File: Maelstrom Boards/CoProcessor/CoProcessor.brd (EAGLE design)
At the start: 101.6 x 101.6 mm, 2 parts, among them U1 STM32F439ZIT6

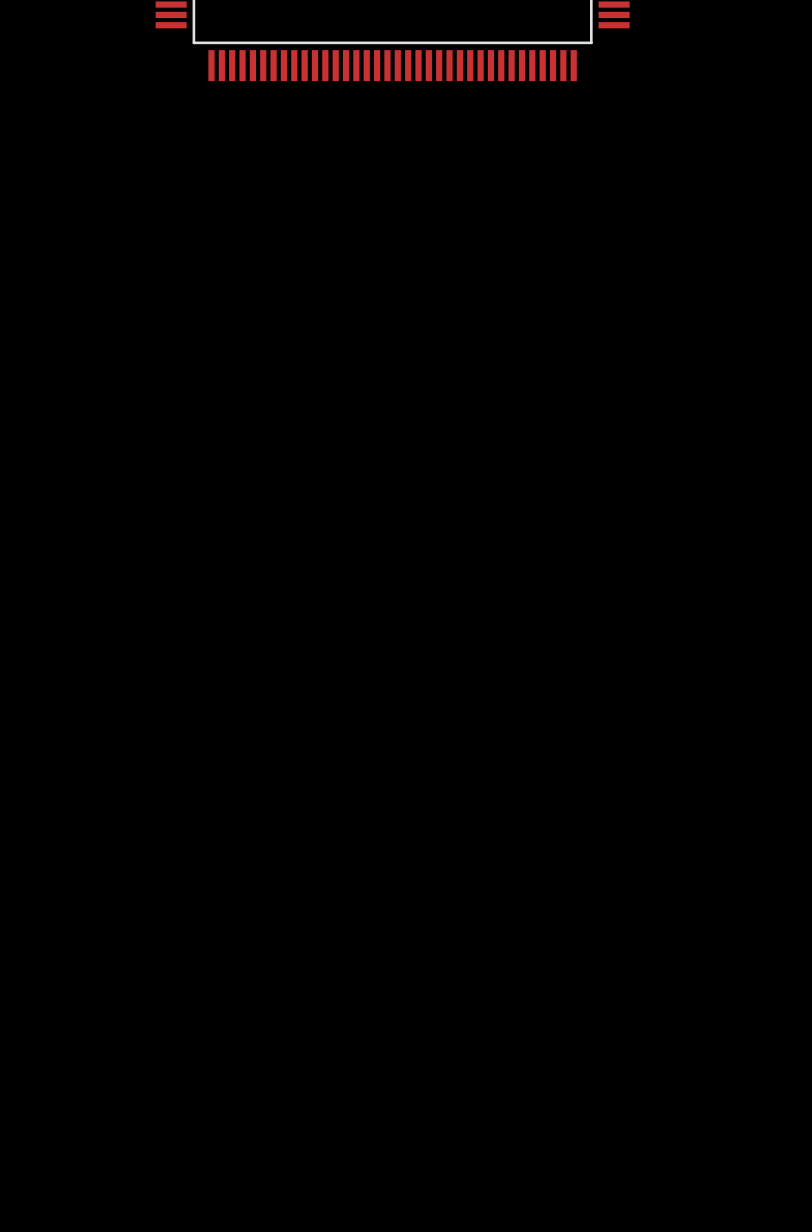
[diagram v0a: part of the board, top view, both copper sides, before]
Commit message: add base copro requirements
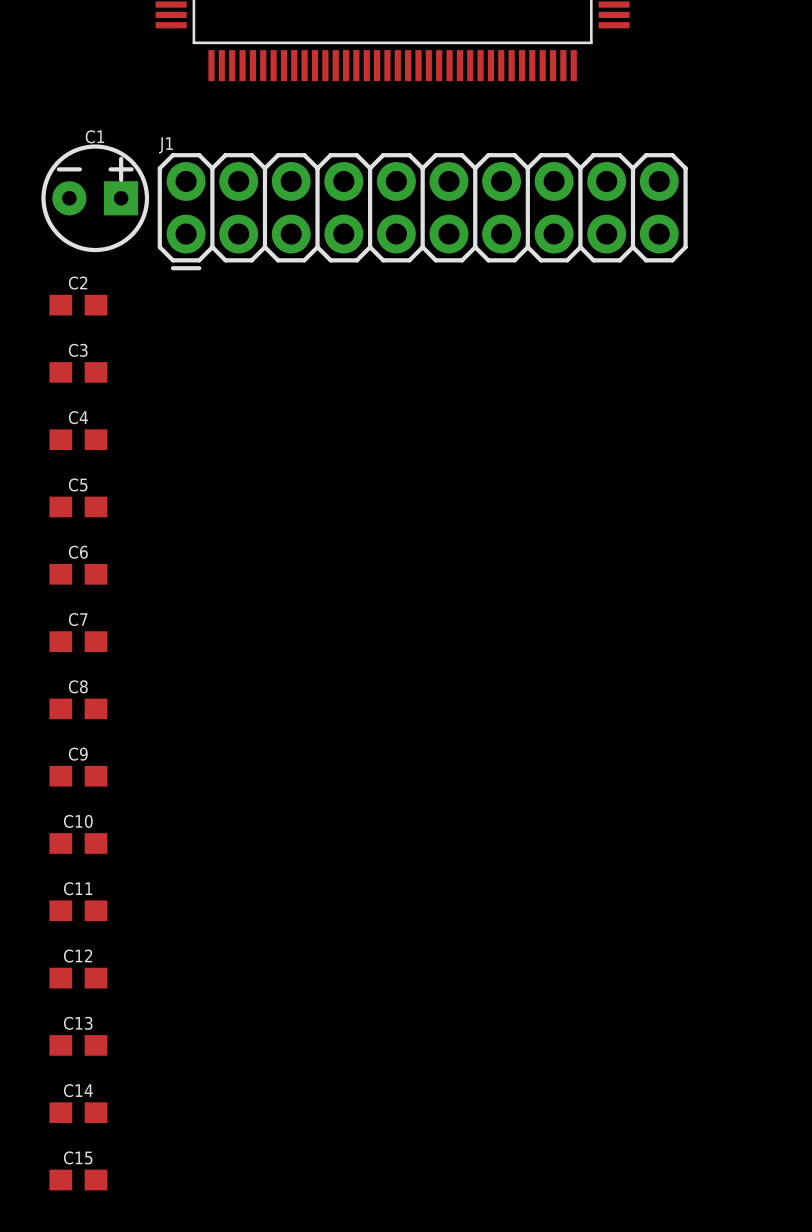
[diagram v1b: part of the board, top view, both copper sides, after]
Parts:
- added C1: 10uF, SparkFun-Capacitors:CPOL-RADIAL-2.5MM-5MM-KIT
- added C10, C11, C12, C13, C2, C3, C4, C5, C6, C7, C8, C9: 0.1uF, SparkFun-Capacitors:0603
- added C14, C15: 2.2uF, SparkFun-Capacitors:0603
- added J1: (no value), SparkFun-Connectors:2X10
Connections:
- removed net VCAP_1: U1.71
- removed net VCAP_2: U1.106
- removed net VDD: U1.108, U1.121, U1.131, U1.144, U1.17, U1.30, U1.39, U1.52, U1.62, U1.72, U1.84, U1.95
- removed net VSS: U1.107, U1.120, U1.130, U1.16, U1.38, U1.51, U1.61, U1.83, U1.94
- new net 3V3PWR: C1.1, C10.1, C11.1, C12.1, C13.1, C2.1, C3.1, C4.1, C5.1, C6.1, C7.1, C8.1, C9.1, J1.1, J1.2, U$1.4, U$1.5, U$1.51, U$1.52, U$1.53, U$1.6, U1.108, U1.121, U1.131, U1.144, U1.17, U1.30, U1.39, U1.52, U1.62, U1.72, U1.84, U1.95
- new net 5VPWR: U$1.1, U$1.2, U$1.3, U$1.54, U$1.55, U$1.56
- new net GND: C1.2, C10.2, C11.2, C12.2, C13.2, C14.2, C15.2, C2.2, C3.2, C4.2, C5.2, C6.2, C7.2, C8.2, C9.2, J1.10, J1.12, J1.14, J1.16, J1.18, J1.20, J1.4, J1.6, J1.8, U$1.48, U$1.49, U$1.50, U$1.7, U$1.8, U$1.9, U1.107, U1.120, U1.130, U1.16, U1.38, U1.51, U1.61, U1.83, U1.94
- new net JTCK: J1.9, U1.109
- new net JTDI: J1.5, U1.110
- new net JTDO: J1.13, U1.133
- new net JTMS: J1.7, U1.105
- new net JTRST: J1.3, U1.134
- new net N$1: C14.1, U1.106
- new net N$2: C15.1, U1.71
- new net NRST: J1.15, U1.25

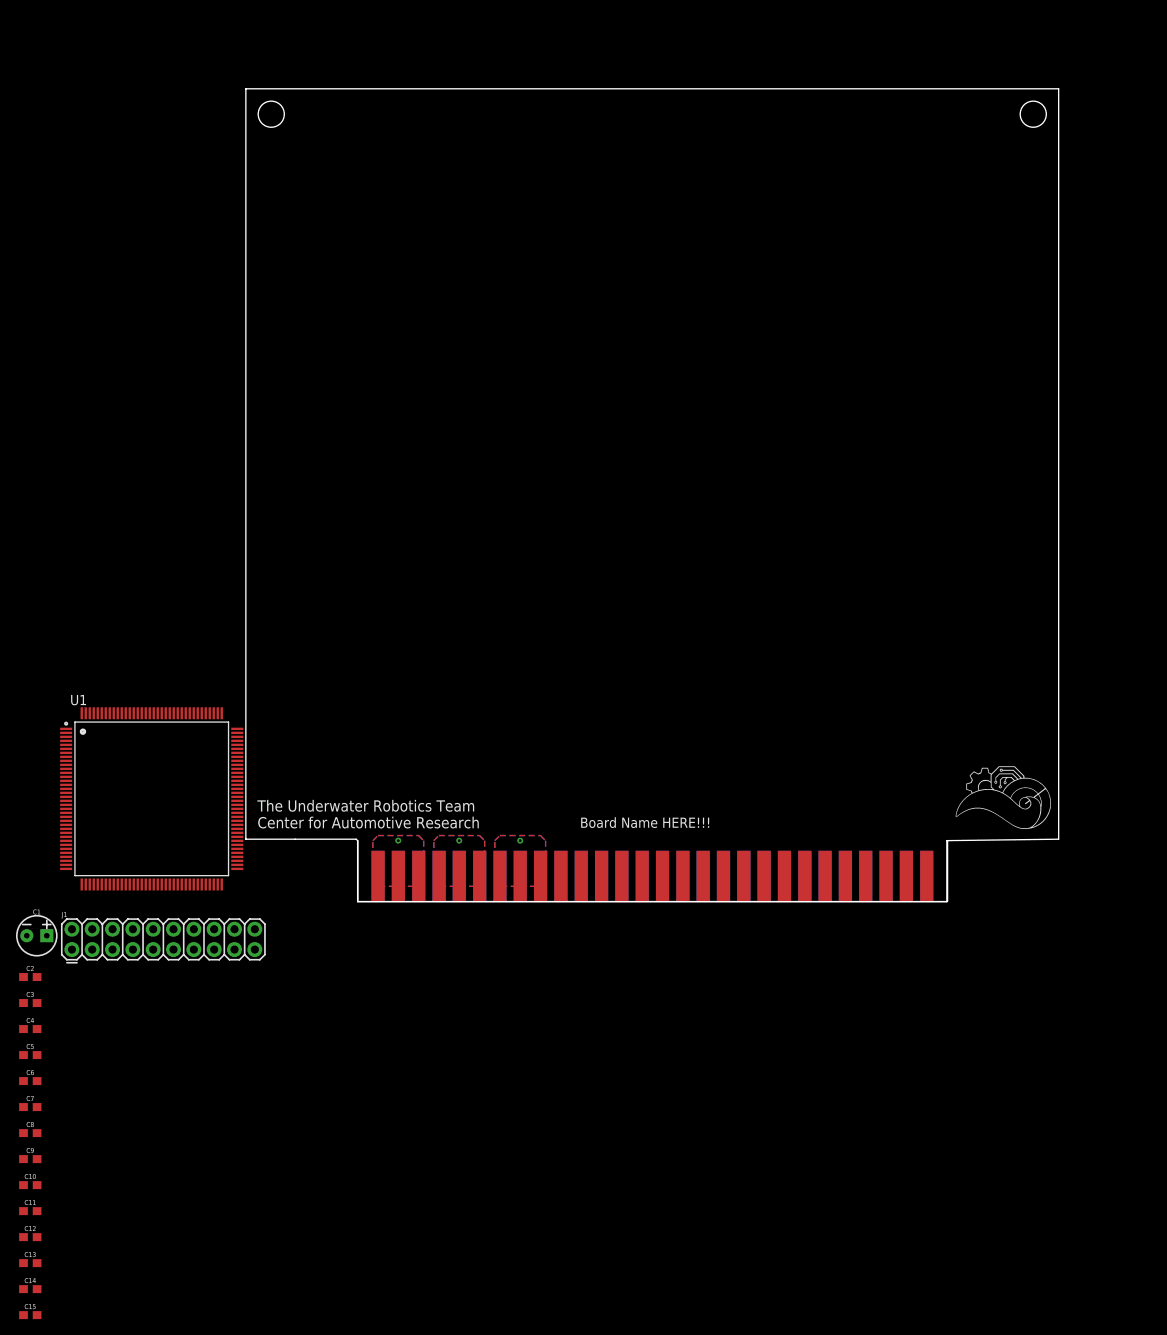
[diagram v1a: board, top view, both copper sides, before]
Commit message: Almost done with schematic, working on board
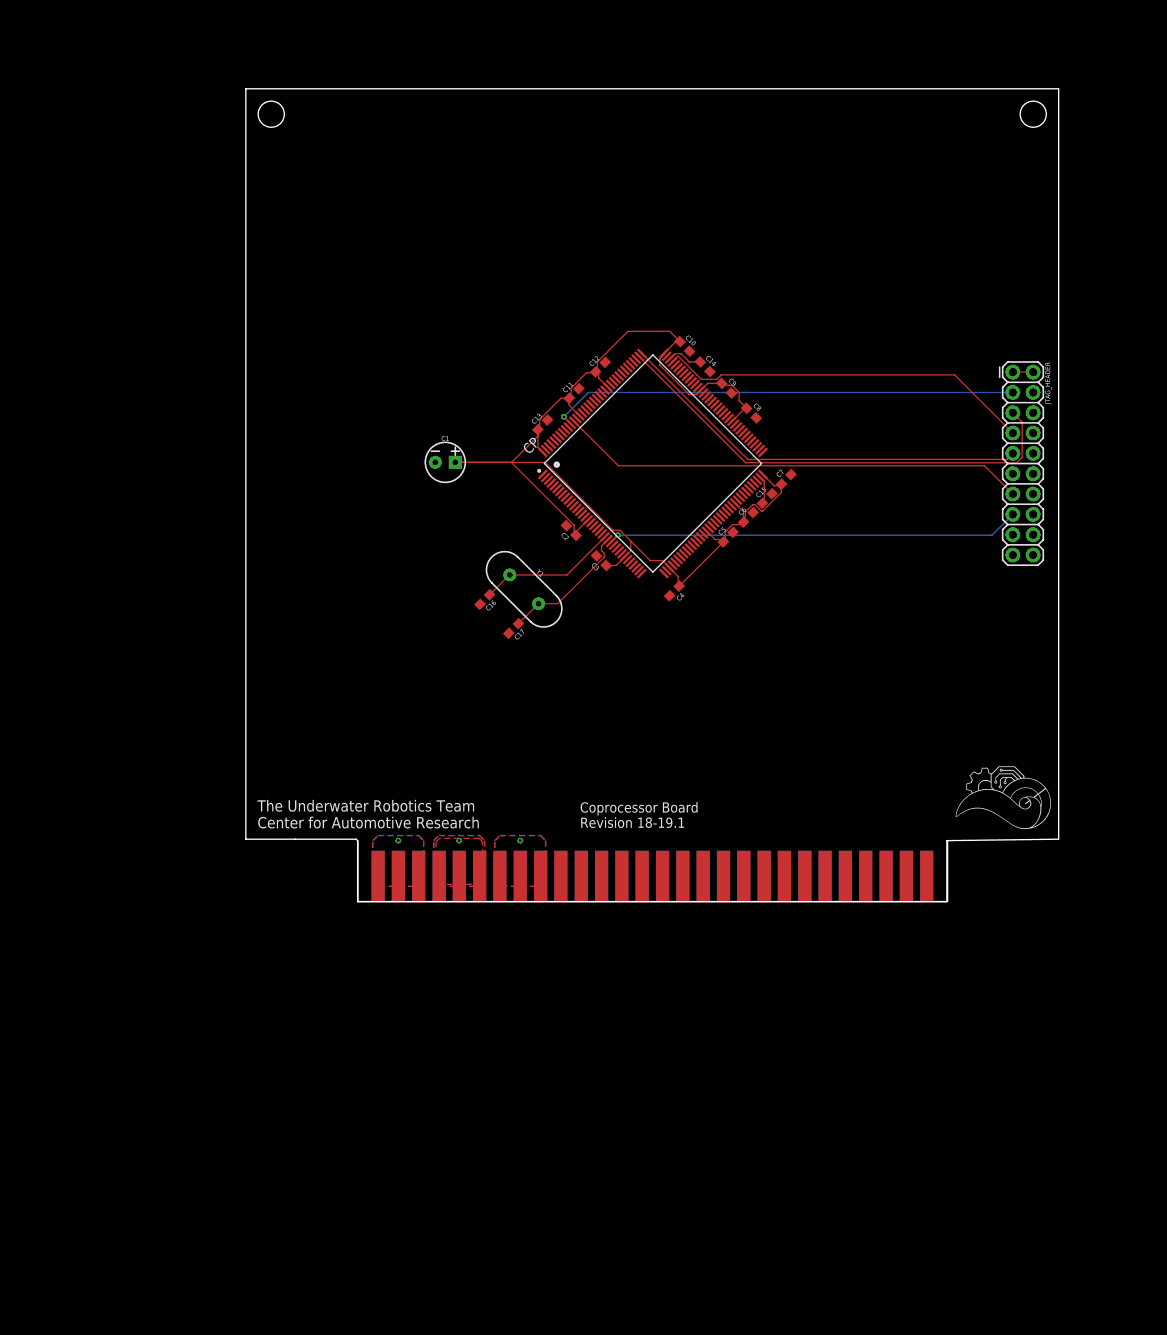
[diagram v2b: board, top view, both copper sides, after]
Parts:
- removed J1: (no value), SparkFun-Connectors:2X10
- removed U1: STM32F439ZIT6, STM32F439ZIT6:QFP50P2200X2200X160-144N
- added C16, C17: 18pF, SparkFun-Capacitors:0603
- added CP: STM32F439ZIT6, STM32F439ZIT6:QFP50P2200X2200X160-144N
- added JTAG_HEADER: (no value), SparkFun-Connectors:2X10
- added Y1: (no value), SparkFun-Clocks:HC49US
- moved C14 142.9 mm to (57.4, 66.9), turned to 315 degrees
- moved C15 137.5 mm to (65.2, 50.4), turned to 45 degrees
- moved C10 133.0 mm to (54.9, 69.4), turned to 315 degrees
- moved C12 130.0 mm to (44.3, 66.8), turned to 45 degrees
- moved C9 129.8 mm to (60.1, 64.2), turned to 315 degrees
- moved C8 127.4 mm to (63.2, 61.1), turned to 315 degrees
- moved C7 122.8 mm to (67.5, 52.8), turned to 45 degrees
- moved C13 122.8 mm to (37.1, 59.6), turned to 45 degrees
- moved C11 122.7 mm to (41.0, 63.5), turned to 45 degrees
- moved C6 114.1 mm to (62.8, 48.0), turned to 45 degrees
- moved C5 108.6 mm to (60.3, 45.6), turned to 45 degrees
- moved C4 97.4 mm to (53.6, 38.8), turned to 225 degrees
- moved C3 90.3 mm to (44.4, 42.6), turned to 135 degrees
- moved C2 87.7 mm to (40.7, 46.4), turned to 135 degrees
- moved C1 78.2 mm to (24.9, 54.9)
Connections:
- new net OSC1: C17.1, CP.24, Y1.2
- new net OSC2: C16.1, CP.23, Y1.1
- net 3V3PWR: now also CP.108, CP.121, CP.131, CP.144, CP.17, CP.30, CP.39, CP.52, CP.62, CP.72, CP.84, CP.95, JTAG_HEADER.1, JTAG_HEADER.2; no longer J1.1, J1.2, U1.108, U1.121, U1.131, U1.144, U1.17, U1.30, U1.39, U1.52, U1.62, U1.72, U1.84, U1.95
- net GND: now also C16.2, C17.2, CP.107, CP.120, CP.130, CP.16, CP.38, CP.51, CP.61, CP.83, CP.94, JTAG_HEADER.10, JTAG_HEADER.12, JTAG_HEADER.14, JTAG_HEADER.16, JTAG_HEADER.18, JTAG_HEADER.20, JTAG_HEADER.4, JTAG_HEADER.6, JTAG_HEADER.8; no longer J1.10, J1.12, J1.14, J1.16, J1.18, J1.20, J1.4, J1.6, J1.8, U1.107, U1.120, U1.130, U1.16, U1.38, U1.51, U1.61, U1.83, U1.94
- net JTCK: now also CP.109, JTAG_HEADER.9; no longer J1.9, U1.109
- net JTDI: now also CP.110, JTAG_HEADER.5; no longer J1.5, U1.110
- net JTDO: now also CP.133, JTAG_HEADER.13; no longer J1.13, U1.133
- net JTMS: now also CP.105, JTAG_HEADER.7; no longer J1.7, U1.105
- net JTRST: now also CP.134, JTAG_HEADER.3; no longer J1.3, U1.134
- net N$1: now also CP.106; no longer U1.106
- net N$2: now also CP.71; no longer U1.71
- net NRST: now also CP.25, JTAG_HEADER.15; no longer J1.15, U1.25
- net PDR_ON: now also CP.143; no longer U1.143
- net VBAT: now also CP.6; no longer U1.6
- net VDDA: now also CP.33; no longer U1.33
- net VREF+: now also CP.32; no longer U1.32
- net VSSA: now also CP.31; no longer U1.31
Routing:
- net 3V3PWR: track 0.00 -> 157.8 mm
- net JTDI: track 0.00 -> 59.7 mm
- net JTRST: track 0.00 -> 58.7 mm, vias 0 -> 1
- net JTDO: track 0.00 -> 58.6 mm
- net JTCK: track 0.00 -> 52.2 mm
- net NRST: track 0.00 -> 51.7 mm, vias 0 -> 1
- net JTMS: track 0.00 -> 47.3 mm
- net OSC2: track 0.00 -> 17.4 mm
- net OSC1: track 0.00 -> 17.0 mm
- net N$1: track 0.00 -> 4.54 mm
- net N$2: track 0.00 -> 3.54 mm
- added copper zone on layer 1, net 3V3PWR
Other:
- board text added: "Coprocessor Board Revision 18-19.1"
- board text removed: "Board Name HERE!!!"

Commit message: Update copro for f405
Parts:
- removed C1: 10uF, SparkFun-Capacitors:CPOL-RADIAL-2.5MM-5MM-KIT
- removed C10, C11, C12, C13, C2, C3, C4, C5, C6, C7, C8, C9: 0.1uF, SparkFun-Capacitors:0603
- removed C14, C15: 2.2uF, SparkFun-Capacitors:0603
- removed C16, C17: 18pF, SparkFun-Capacitors:0603
- removed CP: STM32F439ZIT6, STM32F439ZIT6:QFP50P2200X2200X160-144N
- removed JTAG_HEADER: (no value), SparkFun-Connectors:2X10
- removed Y1: (no value), SparkFun-Clocks:HC49US
- added U1: STM32F405RGT6, STM32F405RGT6:QFP50P1200X1200X160-64N
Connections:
- net 5VPWR renamed +3V3
- removed net 3V3PWR: C1.1, C10.1, C11.1, C12.1, C13.1, C2.1, C3.1, C4.1, C5.1, C6.1, C7.1, C8.1, C9.1, CP.108, CP.121, CP.131, CP.144, CP.17, CP.30, CP.39, CP.52, CP.62, CP.72, CP.84, CP.95, JTAG_HEADER.1, JTAG_HEADER.2, U$1.4, U$1.5, U$1.51, U$1.52, U$1.53, U$1.6
- removed net JTCK: CP.109, JTAG_HEADER.9
- removed net JTDI: CP.110, JTAG_HEADER.5
- removed net JTDO: CP.133, JTAG_HEADER.13
- removed net JTMS: CP.105, JTAG_HEADER.7
- removed net JTRST: CP.134, JTAG_HEADER.3
- removed net N$1: C14.1, CP.106
- removed net N$2: C15.1, CP.71
- removed net NRST: CP.25, JTAG_HEADER.15
- removed net OSC1: C17.1, CP.24, Y1.2
- removed net OSC2: C16.1, CP.23, Y1.1
- removed net PDR_ON: CP.143
- removed net VREF+: CP.32
- new net +5V: U$1.11, U$1.12, U$1.13, U$1.44, U$1.45, U$1.46
- new net 12V_CNTRL: U$1.16
- new net 3V3_CNTRL: U$1.14
- new net 5V_CNTRL: U$1.15
- new net ACOUS_CNTRL: U$1.17
- new net BOARD_SCL: U$1.31
- new net BOARD_SDA: U$1.32
- new net JETS_CNTRL: U$1.18
- new net MOBO_CNTRL: U$1.19
- new net PWM_CH1: U$1.20
- new net PWM_CH2: U$1.21
- new net PWM_CH3: U$1.22
- new net PWM_CH4: U$1.23
- new net PWM_CH5: U$1.24
- new net PWM_CH6: U$1.25
- new net PWM_CH7: U$1.26
- new net PWM_CH8: U$1.27
- new net SENSOR_SCL: U$1.29
- new net SENSOR_SDA: U$1.30
- new net SW_1: U$1.38
- new net SW_2: U$1.39
- new net SW_3: U$1.40
- new net SW_4: U$1.41
- new net SW_5: U$1.42
- new net SW_KILL: U$1.37
- new net VCAP_1: U1.31
- new net VCAP_2: U1.47
- new net VDD: U1.19, U1.32, U1.48, U1.64
- new net VSS: U1.18, U1.63
- net GND: now also U$1.10, U$1.4, U$1.47, U$1.5, U$1.51, U$1.52, U$1.53, U$1.6; no longer C1.2, C10.2, C11.2, C12.2, C13.2, C14.2, C15.2, C16.2, C17.2, C2.2, C3.2, C4.2, C5.2, C6.2, C7.2, C8.2, C9.2, CP.107, CP.120, CP.130, CP.16, CP.38, CP.51, CP.61, CP.83, CP.94, JTAG_HEADER.10, JTAG_HEADER.12, JTAG_HEADER.14, JTAG_HEADER.16, JTAG_HEADER.18, JTAG_HEADER.20, JTAG_HEADER.4, JTAG_HEADER.6, JTAG_HEADER.8, U$1.50, U$1.7
- net VBAT: now also U1.1; no longer CP.6
- net VDDA: now also U1.13; no longer CP.33
- net VSSA: now also U1.12; no longer CP.31
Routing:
- net 3V3PWR: track 157.8 -> 0.00 mm
- net JTDI: track 59.7 -> 0.00 mm
- net JTRST: track 58.7 -> 0.00 mm, vias 1 -> 0
- net JTDO: track 58.6 -> 0.00 mm
- net JTCK: track 52.2 -> 0.00 mm
- net NRST: track 51.7 -> 0.00 mm, vias 1 -> 0
- net JTMS: track 47.3 -> 0.00 mm
- net OSC2: track 17.4 -> 0.00 mm
- net OSC1: track 17.0 -> 0.00 mm
- net N$1: track 4.54 -> 0.00 mm
- net N$2: track 3.54 -> 0.00 mm
- added copper zone on layer 1, net +3V3
- added copper zone on layer 16, net +3V3
- added copper zone on layer 1, net +5V
- added copper zone on layer 16, net +5V
- removed copper zone on layer 1, net 3.3V
- removed copper zone on layer 16, net 3.3V
- removed copper zone on layer 1, net 3V3PWR
- removed copper zone on layer 1, net 5V
- removed copper zone on layer 16, net 5V
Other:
- outline, holes or cut-outs redrawn
- board text added: "Board Name HERE!!!"
- board text removed: "Coprocessor Board Revision 18-19.1"

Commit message: updating copro board
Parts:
- added C1, C2, C3, C4, C7, C8: (no value), rcl:C0603
- added C5: 4.7uF, rcl:C0603
- added C6: 10nF, rcl:C0603
- added D1, D2, D3, D4: (no value), SparkFun-LED:LED-0603
- added J1: USB_MINI-B_SMT, SparkFun-Connectors:USB-MINIB
- added P1: RB1-125BAG1A, RJ45-MAGJACK:WIZNET_RB1-125BAG1A
- added Q1, Q2, Q3, Q4, Q5, Q6, Q7, Q8: 310mA/60V/1.6Ω, SparkFun-DiscreteSemi:SOT323
- added R1, R18, R19, R2: 4.7k, resistor:R0603
- added R10, R14, R15, R16, R17, R3, R4, R5, R6, R7, R8, R9: (no value), rcl:R0603
- added R11: 560, rcl:R0603
- added R12, R13: 22, rcl:R0603
- added R20: 100k, rcl:R0603
- added R21: 12.4k 1%, rcl:R0603
- added R22, R23: 330, rcl:R0603
- added R24: 1M, rcl:R0603
- added U2: STM32F405RGT6, STM32F405RGT6:QFP50P1200X1200X160-64N
- added Y1: 16MHz, SparkFun-Clocks:HC49US
- added Y2: 25MHz, SparkFun-Clocks:HC49US
- U1: value STM32F405RGT6 -> W5500; device STM32F405RGT6:QFP50P1200X1200X160-64N -> W5500:QFP50P900X900X160-48N
- moved U1 59.8 mm to (30.0, 56.5)
- moved U$1 0.10 mm to (15.8, 0.00)
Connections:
- removed net ACOUS_CNTRL: U$1.17
- removed net BOARD_SCL: U$1.31
- removed net BOARD_SDA: U$1.32
- removed net SENSOR_SCL: U$1.29
- removed net SENSOR_SDA: U$1.30
- removed net VCAP_1: U1.31
- removed net VCAP_2: U1.47
- removed net VDD: U1.19, U1.32, U1.48, U1.64
- removed net VDDA: U1.13
- removed net VSS: U1.18, U1.63
- removed net VSSA: U1.12
- new net ACOU_CNTRL: U$1.17, U2.9
- new net BP_SCL: R1.1, U$1.31, U2.58
- new net BP_SDA: R2.1, U$1.32, U2.59
- new net LED_BLUE: R17.1, U2.56
- new net LED_GREEN: R16.1, U2.50
- new net LED_RED: R14.1, U2.46
- new net LED_YELLOW: R15.1, U2.49
- new net N$1: C1.1, U2.6, Y1.1
- new net N$10: C4.2, U2.47
- new net N$11: C3.2, U2.31
- new net N$12: C5.1, U1.20
- new net N$13: C6.1, U1.22
- new net N$14: R21.2, U1.10
- new net N$16: P1.R2, U1.1
- new net N$17: P1.R1, U1.2
- new net N$18: P1.R8, U1.5
- new net N$19: P1.R7, U1.6
- new net N$2: J1.ID, R11.1
- new net N$20: P1.L2, R22.2
- new net N$21: P1.L4, R23.2
- new net N$22: R22.1, U1.27
- new net N$23: R23.1, U1.25
- new net N$24: C8.1, R24.2, U1.30, Y2.2
- new net N$25: C7.1, R24.1, U1.31, Y2.1
- new net N$3: D1.A, R14.2
- new net N$4: J1.D+, R12.1
- new net N$5: J1.D-, R13.1
- new net N$6: D2.A, R15.2
- new net N$7: D3.A, R16.2
- new net N$8: D4.A, R17.2
- new net N$9: C2.1, U2.5, Y1.2
- new net PWM_3V3_CH1: Q1.2, U2.61
- new net PWM_3V3_CH2: Q2.2, U2.62
- new net PWM_3V3_CH3: Q3.2, U2.35
- new net PWM_3V3_CH4: Q4.2, U2.36
- new net PWM_3V3_CH5: Q5.2, U2.14
- new net PWM_3V3_CH6: Q6.2, U2.15
- new net PWM_3V3_CH7: Q7.2, U2.16
- new net PWM_3V3_CH8: Q8.2, U2.17
- new net ROBOT_SCL: R18.1, U$1.29, U2.29
- new net ROBOT_SDA: R19.1, U$1.30, U2.30
- new net SPI_MISO: U2.22
- new net SPI_MOSI: U2.23
- new net SPI_SCK: U2.21
- new net SPI_SS: U2.20
- new net USB_DN: R13.2
- new net USB_DP: R12.2
- new net USB_ID: R11.2, R20.1
- new net VBUS: J1.VBUS
- net +3V3: now also P1.L1, P1.L3, Q1.1, Q2.1, Q3.1, Q4.1, Q5.1, Q6.1, Q7.1, Q8.1, R1.2, R18.2, R19.2, R2.2, R20.2, U1.11, U1.15, U1.17, U1.21, U1.28, U1.4, U1.8, U2.13, U2.19, U2.32, U2.48, U2.64
- net +5V: now also R10.2, R3.2, R4.2, R5.2, R6.2, R7.2, R8.2, R9.2
- net 12V_CNTRL: now also U2.26
- net 3V3_CNTRL: now also U2.8
- net 5V_CNTRL: now also U2.2
- net GND: now also C1.2, C2.2, C3.1, C4.1, C5.2, C6.2, C7.2, C8.2, D1.C, D2.C, D3.C, D4.C, J1.GND, R21.1, U1.14, U1.16, U1.19, U1.29, U1.3, U1.48, U1.9, U2.12, U2.18, U2.63
- net JETS_CNTRL: now also U2.11
- net MOBO_CNTRL: now also U2.10
- net PWM_CH1: now also Q1.3, R3.1
- net PWM_CH2: now also Q2.3, R4.1
- net PWM_CH3: now also Q3.3, R5.1
- net PWM_CH4: now also Q4.3, R6.1
- net PWM_CH5: now also Q5.3, R7.1
- net PWM_CH6: now also Q6.3, R8.1
- net PWM_CH7: now also Q7.3, R9.1
- net PWM_CH8: now also Q8.3, R10.1
- net SW_1: now also U2.34
- net SW_2: now also U2.37
- net SW_3: now also U2.38
- net SW_4: now also U2.24
- net SW_5: now also U2.27
- net SW_KILL: now also U2.33
- net VBAT: now also U2.1; no longer U1.1
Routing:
- net +3V3: track 0.00 -> 157.7 mm, vias 1 -> 7
- net ROBOT_SCL: track 0.00 -> 89.7 mm, vias 0 -> 2
- net ROBOT_SDA: track 0.00 -> 86.8 mm, vias 0 -> 2
- net BP_SCL: track 0.00 -> 80.7 mm, vias 0 -> 2
- net BP_SDA: track 0.00 -> 75.6 mm, vias 0 -> 2
- net PWM_3V3_CH8: track 0.00 -> 74.6 mm, vias 0 -> 1
- net +5V: track 0.00 -> 69.6 mm, vias 1 -> 12
- net PWM_3V3_CH7: track 0.00 -> 66.6 mm, vias 0 -> 1
- net PWM_3V3_CH6: track 0.00 -> 62.9 mm, vias 0 -> 1
- net PWM_3V3_CH5: track 0.00 -> 55.9 mm, vias 0 -> 5
- net PWM_3V3_CH2: track 0.00 -> 45.6 mm, vias 0 -> 3
- net SW_KILL: track 0.00 -> 40.4 mm
- net SW_3: track 0.00 -> 38.9 mm, vias 0 -> 2
- net PWM_3V3_CH4: track 0.00 -> 37.7 mm, vias 0 -> 1
- net PWM_3V3_CH1: track 0.00 -> 37.6 mm, vias 0 -> 3
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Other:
- board text added: "Coprocessor"
- board text removed: "Board Name HERE!!!"
